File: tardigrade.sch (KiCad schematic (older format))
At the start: 0 parts

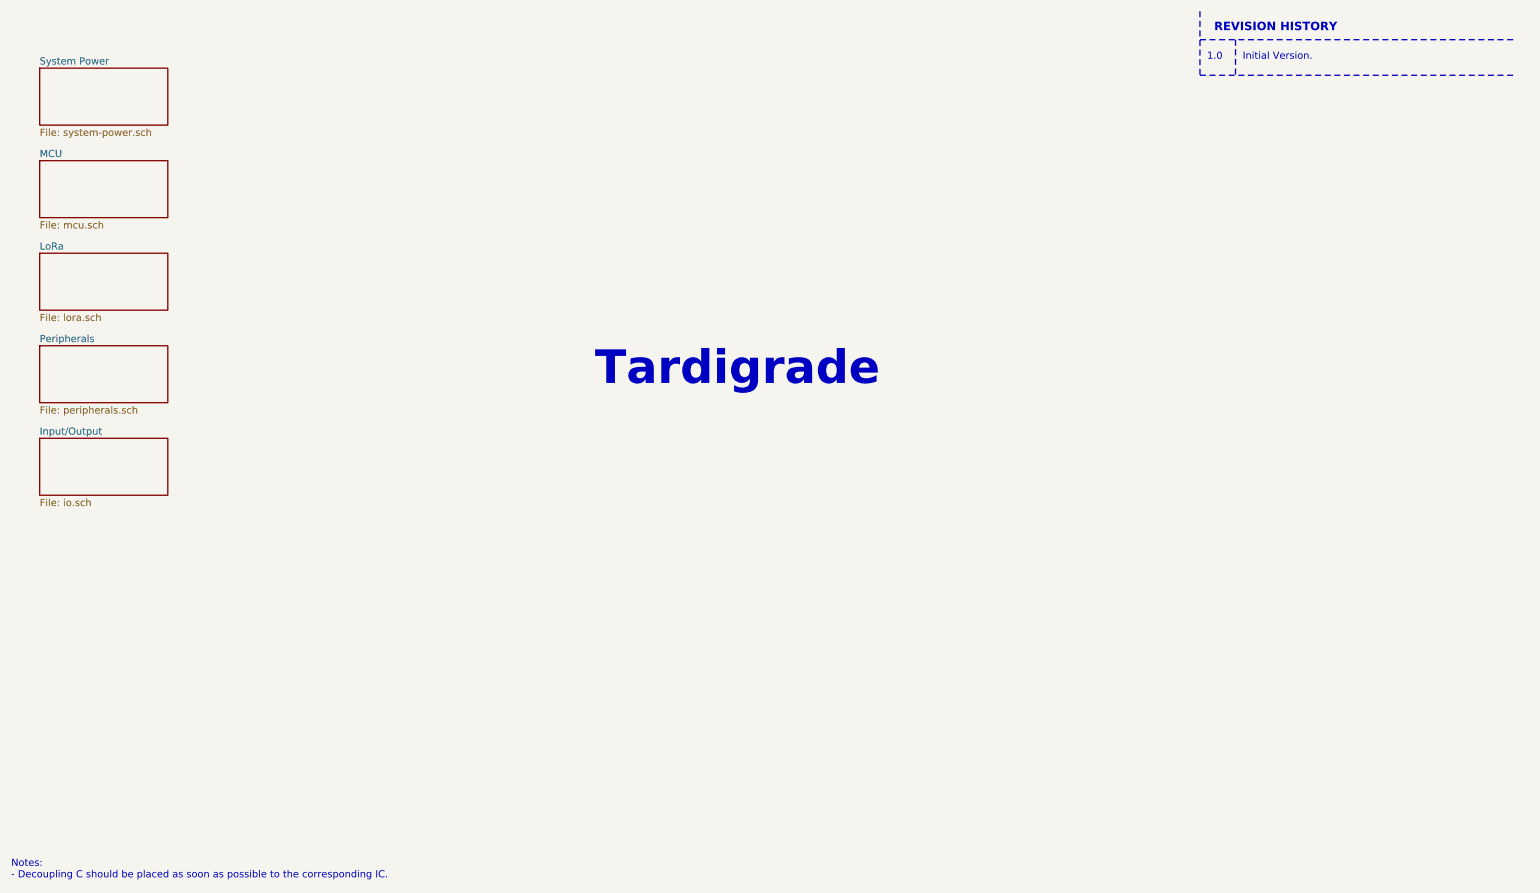
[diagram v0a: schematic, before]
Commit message: Added revision comment on schema
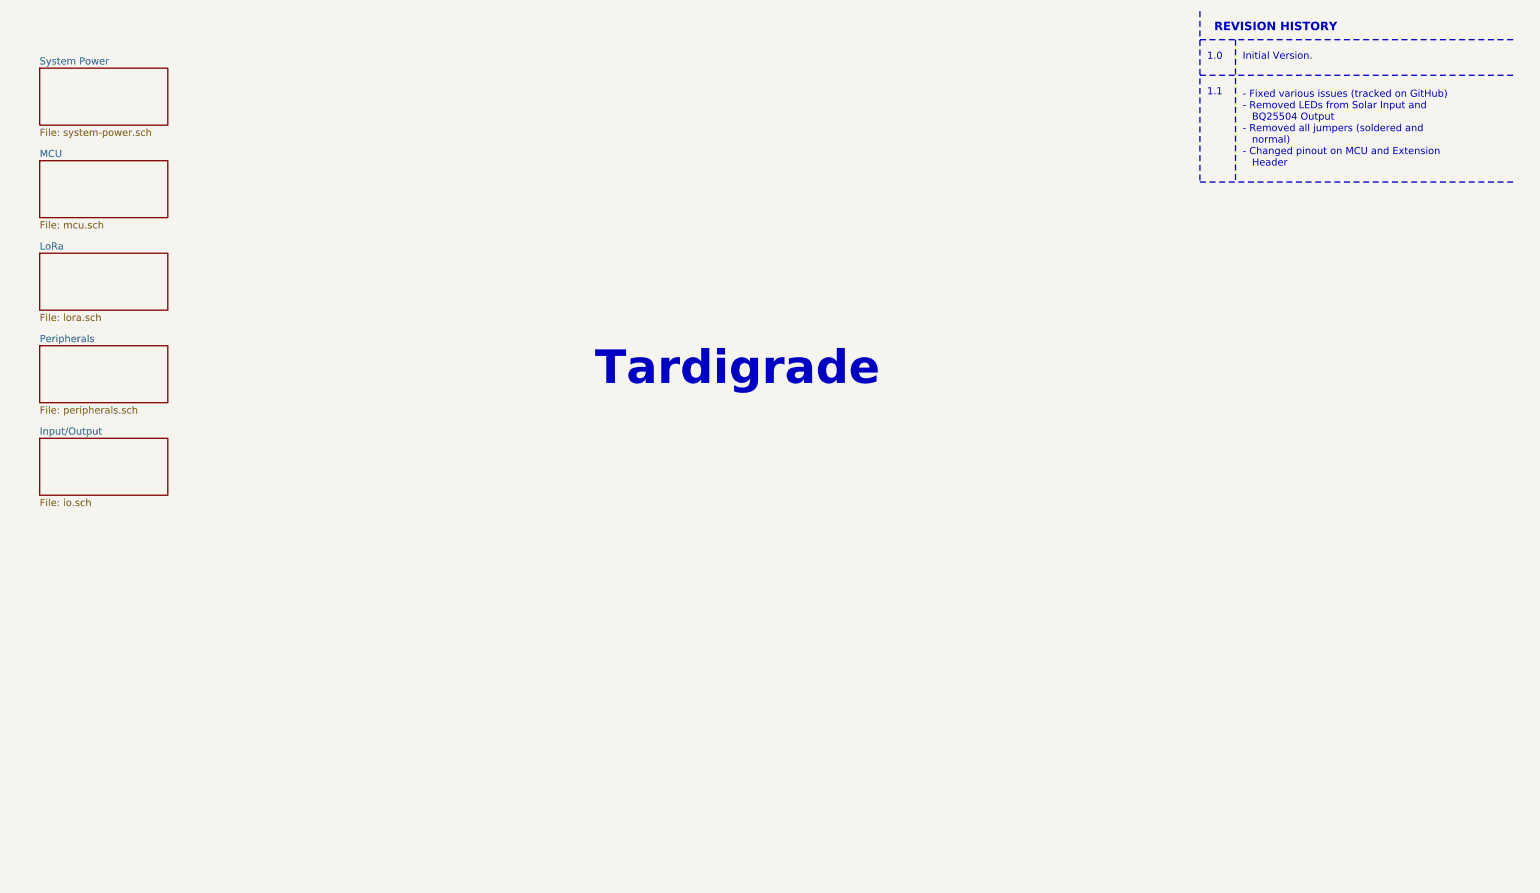
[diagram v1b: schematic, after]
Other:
- note added: "- Fixed various issues (tracked on GitHub)\n- Removed LEDs from Solar Input and \n BQ25504 Output\n- Removed all jumpers (soldered and \n normal)\n- Changed pinout on MCU and Extension \n Header"
- note added: "1.1"
- note removed: "Notes: \n- Decoupling C should be placed as soon as possible to the corresponding IC."
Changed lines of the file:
@@
 	9000 950  11200 950
 Wire Notes Line
-	9000 500  9000 950
-Wire Notes Line
-	9250 700  9250 950
+	9000 500  9000 1700
 Text Notes 4750 3150 0    236  ~ 47
 Tardigrade
@@
 F1 "io.sch" 50
 $EndSheet
-Text Notes 650  6600 0    50   ~ 0
-Notes: \n- Decoupling C should be placed as soon as possible to the corresponding IC.
+Text Notes 9300 1600 0    50   ~ 0
+- Fixed various issues (tracked on GitHub)\n- Removed LEDs from Solar Input and \n   BQ25504 Output\n- Removed all jumpers (soldered and \n   normal)\n- Changed pinout on MCU and Extension \n   Header
+Wire Notes Line
+	9000 1700 11200 1700
+Wire Notes Line
+	9250 700  9250 1700
+Text Notes 9050 1100 0    50   ~ 0
+1.1
 $EndSCHEMATC
